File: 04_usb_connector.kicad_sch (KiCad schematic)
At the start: 11 parts

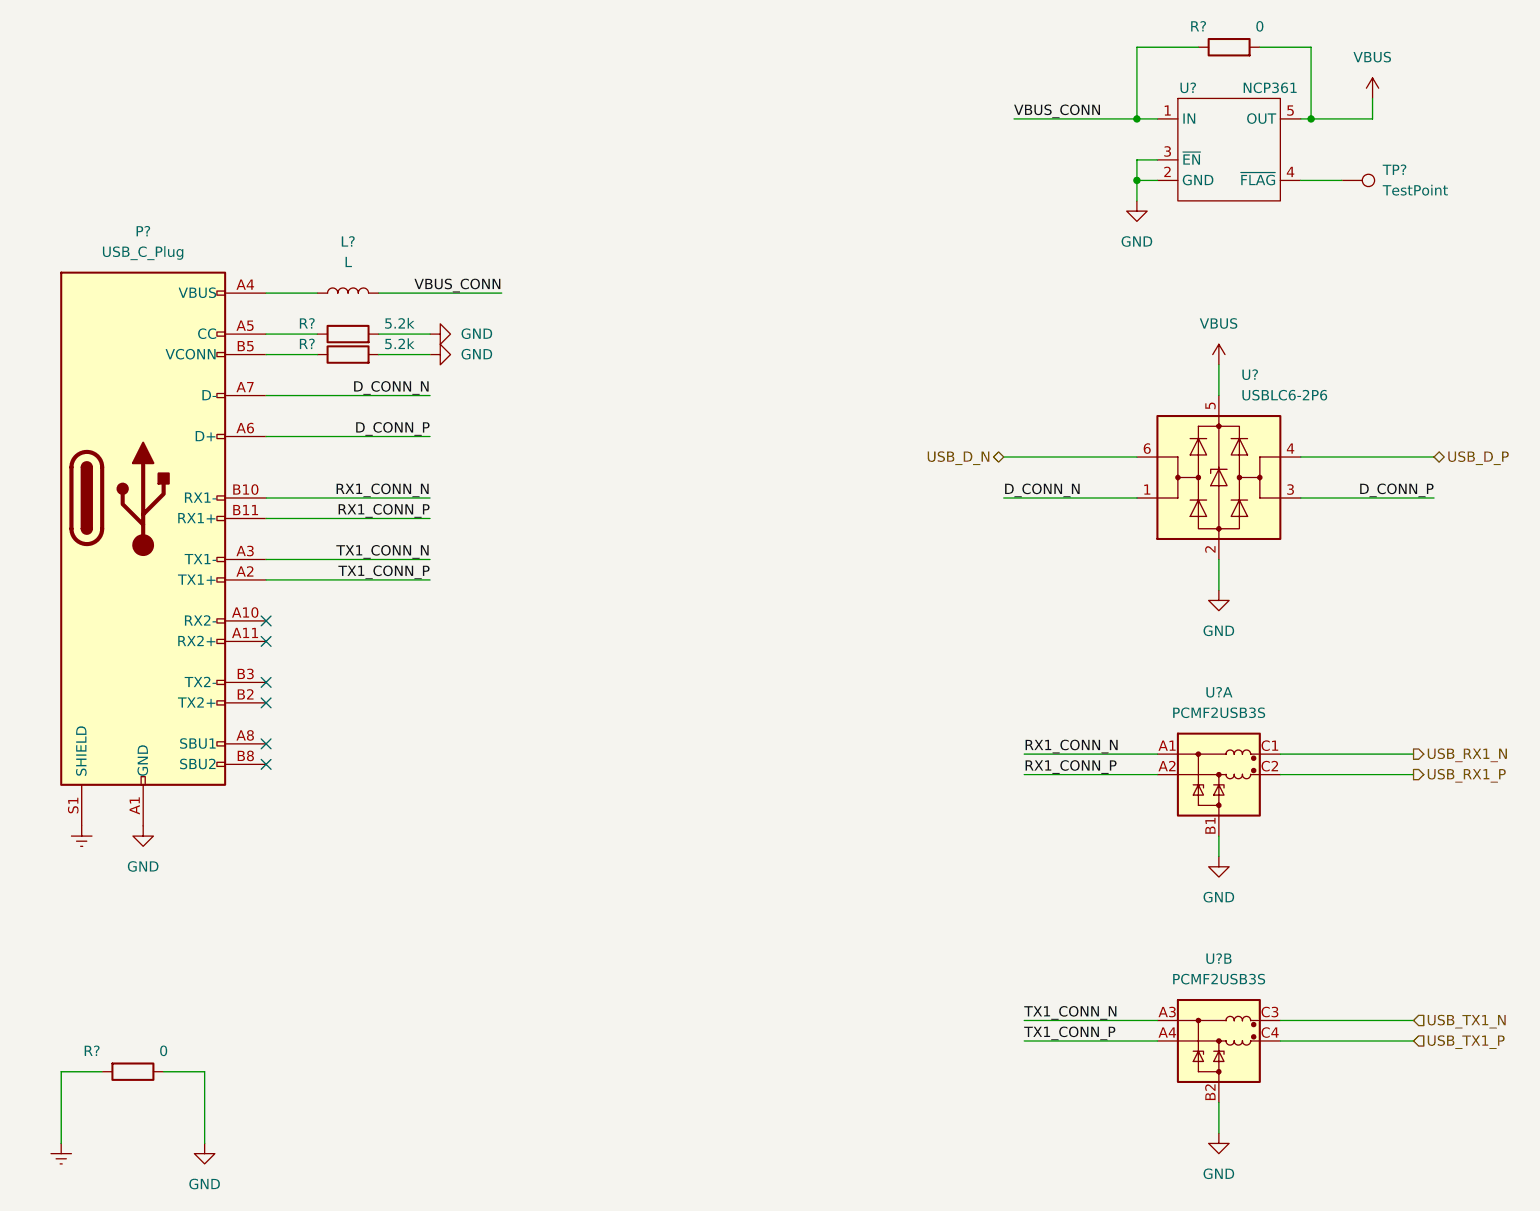
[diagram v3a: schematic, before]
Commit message: cleaned up some DRC errors
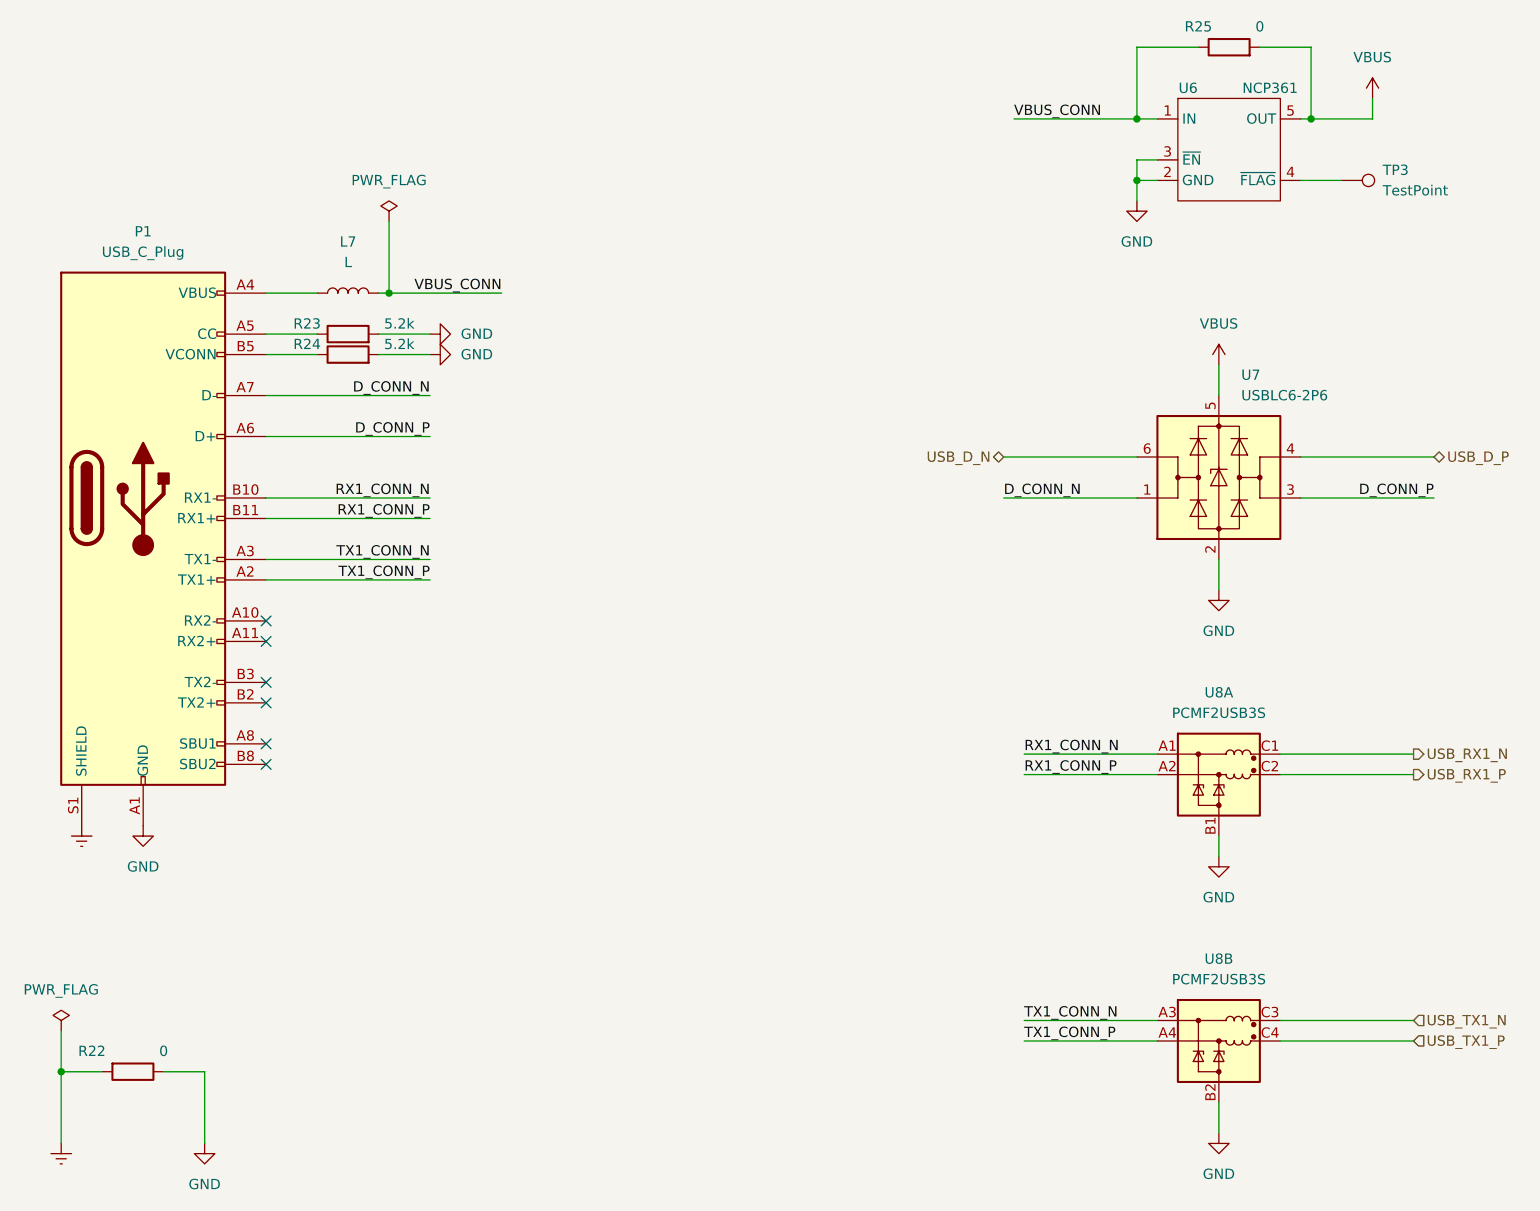
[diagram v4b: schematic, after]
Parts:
- gave numbers to parts that had none: 10

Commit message: finished schematics
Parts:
- L7: value L -> 15uH
- R25: footprint (none) -> Resistor_SMD:R_0603_1608Metric
- TP3: footprint (none) -> TestPoint:TestPoint_THTPad_D1.0mm_Drill0.5mm
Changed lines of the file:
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@@
     (in_bom yes) (on_board yes) (fields_autoplaced)
     (property "Reference" "L7" (id 0) (at 96.52 49.53 90))
-    (property "Value" "L" (id 1) (at 96.52 52.07 90))
+    (property "Value" "15uH" (id 1) (at 96.52 52.07 90))
     (property "Footprint" "Inductor_SMD:L_0603_1608Metric" (id 2) (at 96.52 55.88 0)
       (effects (font (size 1.27 1.27)) hide)
@@
       (effects (font (size 1.27 1.27)) (justify left))
     )
-    (property "Footprint" "" (id 2) (at 219.71 46.99 0)
+    (property "Footprint" "TestPoint:TestPoint_THTPad_D1.0mm_Drill0.5mm" (id 2) (at 219.71 46.99 0)
       (effects (font (size 1.27 1.27)) hide)
     )
@@
     (property "Reference" "R25" (id 0) (at 201.93 22.86 90))
     (property "Value" "0" (id 1) (at 209.55 22.86 90))
-    (property "Footprint" "" (id 2) (at 205.74 27.178 90)
-      (effects (font (size 1.27 1.27)) hide)
-    )
+    (property "Footprint" "Resistor_SMD:R_0603_1608Metric" (id 2) (at 205.74 27.178 90)
+      (effects (font (size 1.27 1.27)) hide)
+    )
